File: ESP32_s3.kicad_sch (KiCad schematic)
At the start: 74 parts, among them J1 Conn_01x02_Pin, J11 backup, J12 Conn_01x02_Pin, J13 Jetson Power Supply, J14 TXRX, J15 TXRX2, J2 programming header usb, J3 Conn_01x02, J4 Servo motor, J5 PJ-040DH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

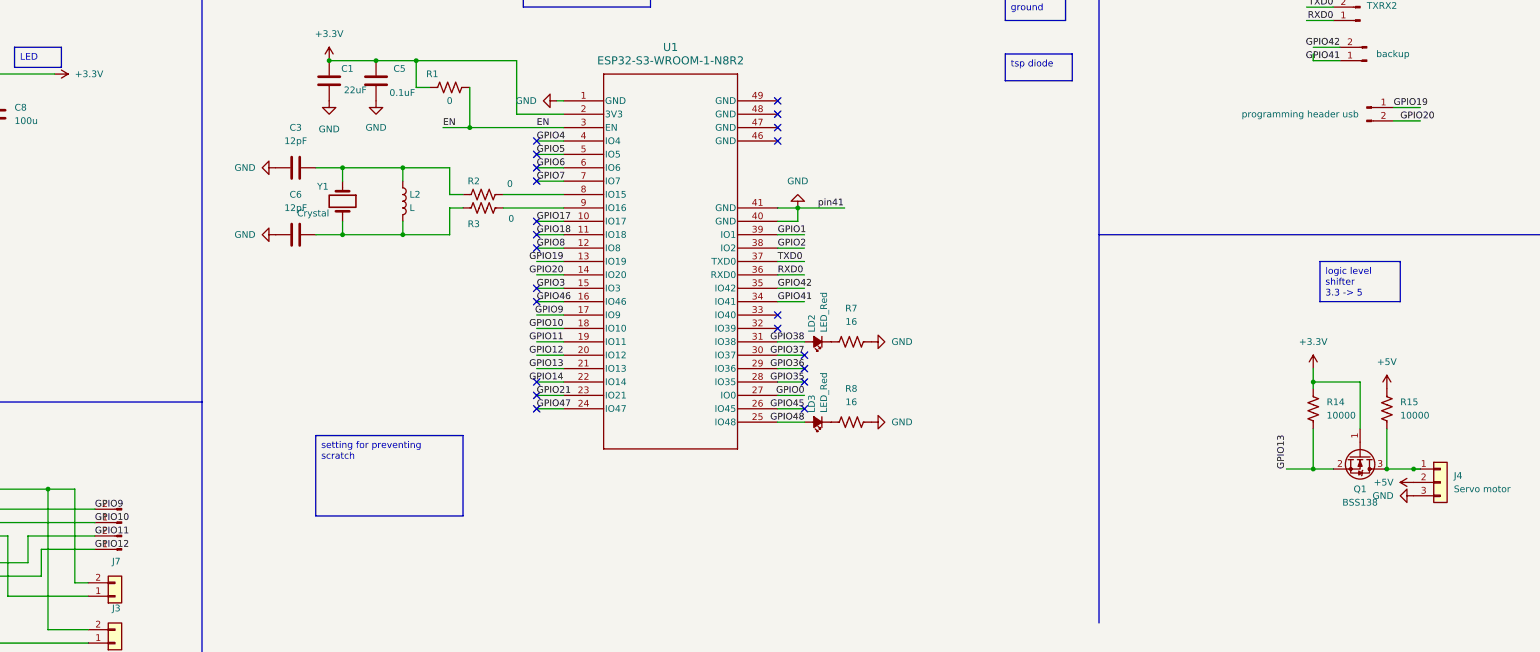
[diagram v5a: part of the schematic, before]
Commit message: small fix of connector and LM1117 footprint
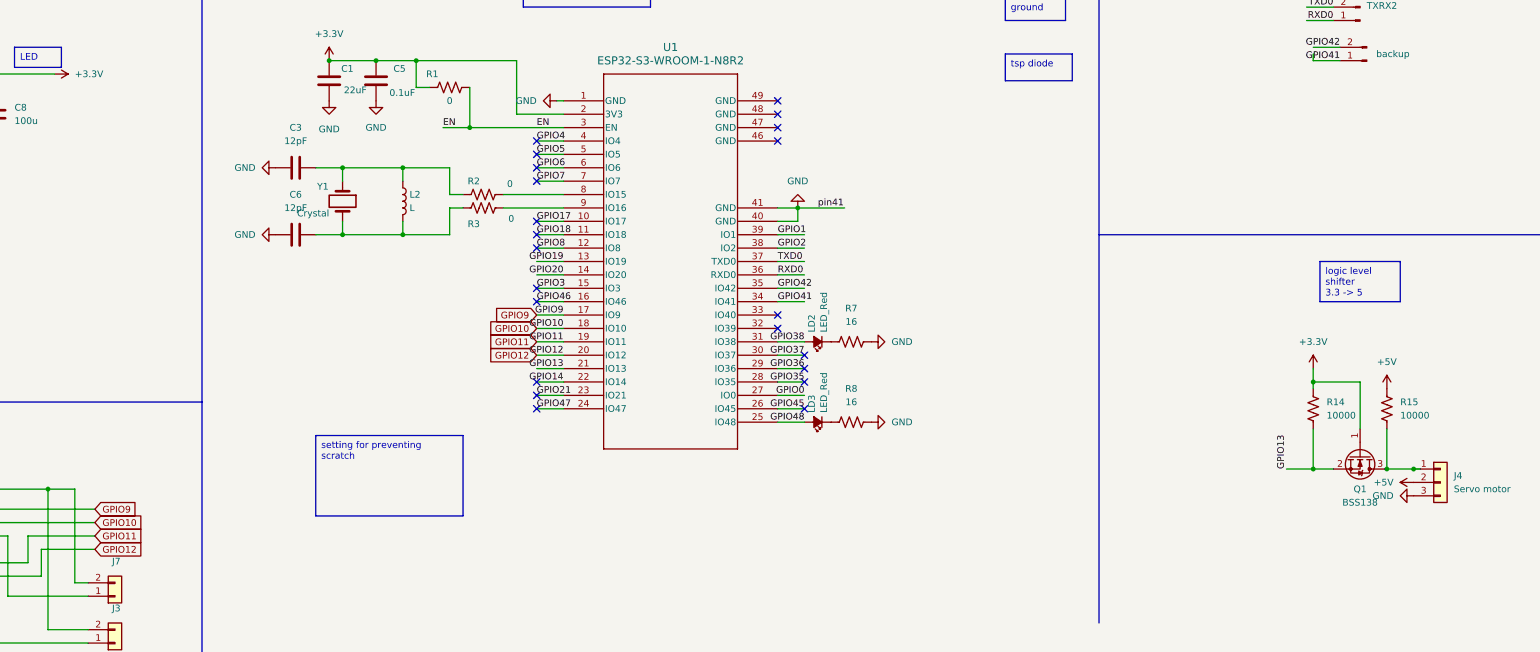
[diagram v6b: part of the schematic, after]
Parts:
- removed J1, J12: Conn_01x02_Pin, 01x02connector:CONN_61300211121_WRE, symbol Connector:Conn_01x02_Pin
- removed J2: programming header usb, 01x02connector:CONN_61300211121_WRE, symbol Connector:Conn_01x02_Pin
- U2: footprint Package_TO_SOT_THT:TO-220-3_Horizontal_TabDown -> LM1117T-ADJ:TO254P1054X470X1955-3

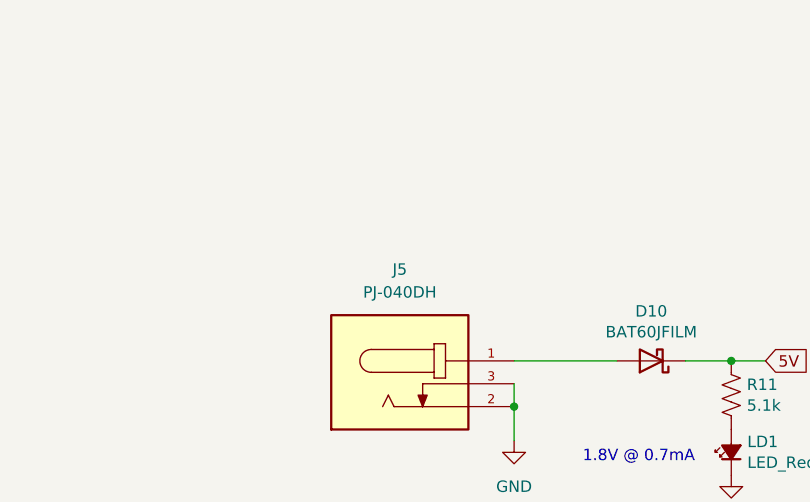
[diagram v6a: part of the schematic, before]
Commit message: fix acute angles
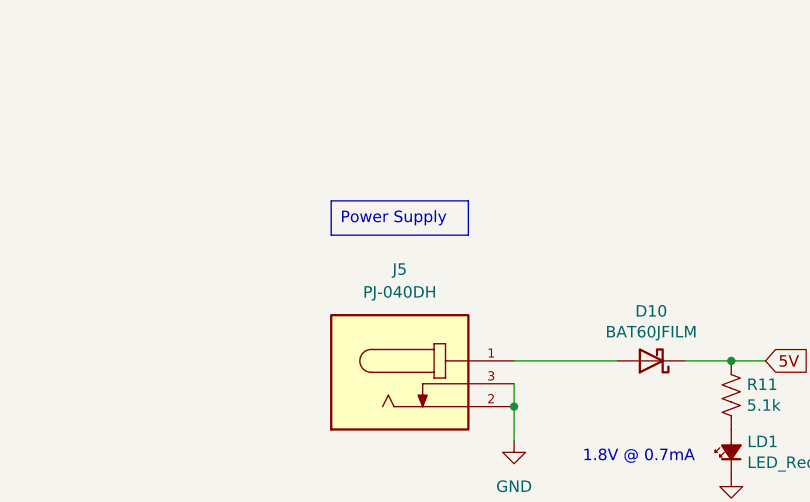
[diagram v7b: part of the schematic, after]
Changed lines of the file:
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@@
+		)
+	)
+	(text_box "Power Supply"
+		(exclude_from_sim no)
+		(at 48.26 31.75 0)
+		(size 15.24 3.81)
+		(stroke
+			(width 0)
+			(type default)
+		)
+		(fill
+			(type none)
+		)
+		(effects
+			(font
+				(size 1.27 1.27)
+			)
+			(justify left top)
 		)
 	)

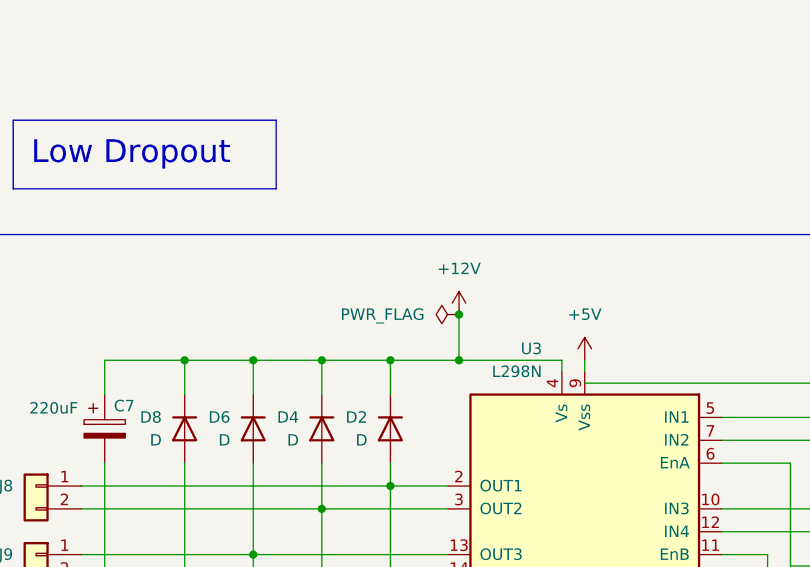
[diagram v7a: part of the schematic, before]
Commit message: fix hbridge input voltage
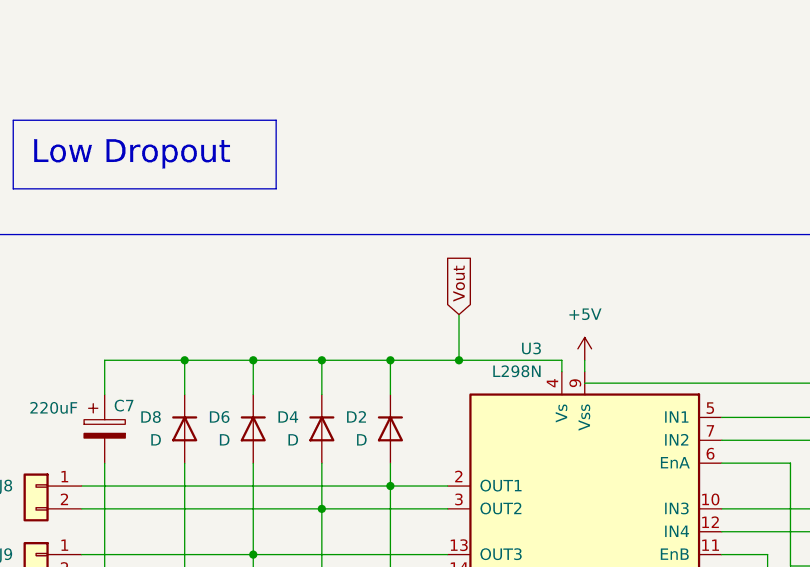
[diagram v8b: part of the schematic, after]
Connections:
- net +12V is gone; now on net Vout: C7.1, D2.1 (K), D4.1 (K), D6.1 (K), D8.1 (K), U3.4 (Vs)
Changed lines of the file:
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@@
 	)
 	(junction
-		(at 66.04 220.98)
-		(diameter 0)
-		(color 0 0 0 0)
-	)
-	(junction
 		(at 100.33 149.86)
 		(diameter 0)
@@
 		)
 	)
+	(global_label "Vout"
+		(shape input)
+		(at 66.04 220.98 90)
+		(fields_autoplaced yes)
+		(effects
+			(font
+				(size 1.27 1.27)
+			)
+			(justify left)
+		)
+		(property "Intersheetrefs" "${INTERSHEET_REFS}"
+			(at 66.04 213.8825 90)
+			(effects
+				(font
+					(size 1.27 1.27)
+				)
+				(justify left)
+				(hide yes)
+			)
+		)
+	)
 	(global_label "5V"
 		(shape input)
@@
 	)
 	(symbol
-		(lib_id "power:PWR_FLAG")
-		(at 66.04 220.98 90)
-		(unit 1)
-		(exclude_from_sim no)
-		(in_bom yes)
-		(on_board yes)
-		(dnp no)
-		(fields_autoplaced yes)
-		(property "Reference" "#FLG01"
-			(at 64.135 220.98 0)
-			(effects
-				(font
-					(size 1.27 1.27)
-				)
-				(hide yes)
-			)
-		)
-		(property "Value" "PWR_FLAG"
-			(at 62.23 220.9799 90)
-			(effects
-				(font
-					(size 1.27 1.27)
-				)
-				(justify left)
-			)
-		)
-		(property "Footprint" ""
-			(at 66.04 220.98 0)
-			(effects
-				(font
-					(size 1.27 1.27)
-				)
-				(hide yes)
-			)
-		)
-		(property "Datasheet" "~"
-			(at 66.04 220.98 0)
-			(effects
-				(font
-					(size 1.27 1.27)
-				)
-				(hide yes)
-			)
-		)
-		(property "Description" "Special symbol for telling ERC where power comes from"
-			(at 66.04 220.98 0)
-			(effects
-				(font
-					(size 1.27 1.27)
-				)
-				(hide yes)
-			)
-		)
-		(pin "1"
-		)
-		(instances
-			(project ""
-				(path "/17b1a26b-4dd3-45da-ac9f-9f7d4372170f"
-					(reference "#FLG01")
-					(unit 1)
-				)
-			)
-		)
-	)
-	(symbol
 		(lib_id "power:GND")
 		(at 163.83 154.94 0)
@@
 		)
 		(instances
-			(project ""
+			(project "ESP32_s3"
 				(path "/17b1a26b-4dd3-45da-ac9f-9f7d4372170f"
 					(reference "#PWR017")
@@
 		)
 		(instances
-			(project ""
+			(project "ESP32_s3"
 				(path "/17b1a26b-4dd3-45da-ac9f-9f7d4372170f"
 					(reference "R7")
@@
 		)
 		(instances
-			(project ""
+			(project "ESP32_s3"
 				(path "/17b1a26b-4dd3-45da-ac9f-9f7d4372170f"
 					(reference "J14")
@@
 	)
 	(symbol
-		(lib_id "power:+12V")
-		(at 66.04 220.98 0)
-		(unit 1)
-		(exclude_from_sim no)
-		(in_bom yes)
-		(on_board yes)
-		(dnp no)
-		(fields_autoplaced yes)
-		(property "Reference" "#PWR024"
-			(at 66.04 224.79 0)
-			(effects
-				(font
-					(size 1.27 1.27)
-				)
-				(hide yes)
-			)
-		)
-		(property "Value" "+12V"
-			(at 66.04 215.9 0)
-			(effects
-				(font
-					(size 1.27 1.27)
-				)
-			)
-		)
-		(property "Footprint" ""
-			(at 66.04 220.98 0)
-			(effects
-				(font
-					(size 1.27 1.27)
-				)
-				(hide yes)
-			)
-		)
-		(property "Datasheet" ""
-			(at 66.04 220.98 0)
-			(effects
-				(font
-					(size 1.27 1.27)
-				)
-				(hide yes)
-			)
-		)
-		(property "Description" "Power symbol creates a global label with name \"+12V\""
-			(at 66.04 220.98 0)
-			(effects
-				(font
-					(size 1.27 1.27)
-				)
-				(hide yes)
-			)
-		)
-		(pin "1"
-		)
-		(instances
-			(project ""
-				(path "/17b1a26b-4dd3-45da-ac9f-9f7d4372170f"
-					(reference "#PWR024")
-					(unit 1)
-				)
-			)
-		)
-	)
-	(symbol
 		(lib_id "Connector:Conn_01x03_Pin")
 		(at 359.41 137.16 180)
@@
 		)
 		(instances
-			(project ""
+			(project "ESP32_s3"
 				(path "/17b1a26b-4dd3-45da-ac9f-9f7d4372170f"
 					(reference "#PWR027")
